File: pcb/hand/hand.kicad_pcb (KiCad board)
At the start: 2 copper layers, 178.2 x 125.2 mm, 43 parts, among them J1 Conn_01x15, J2 Conn_01x15

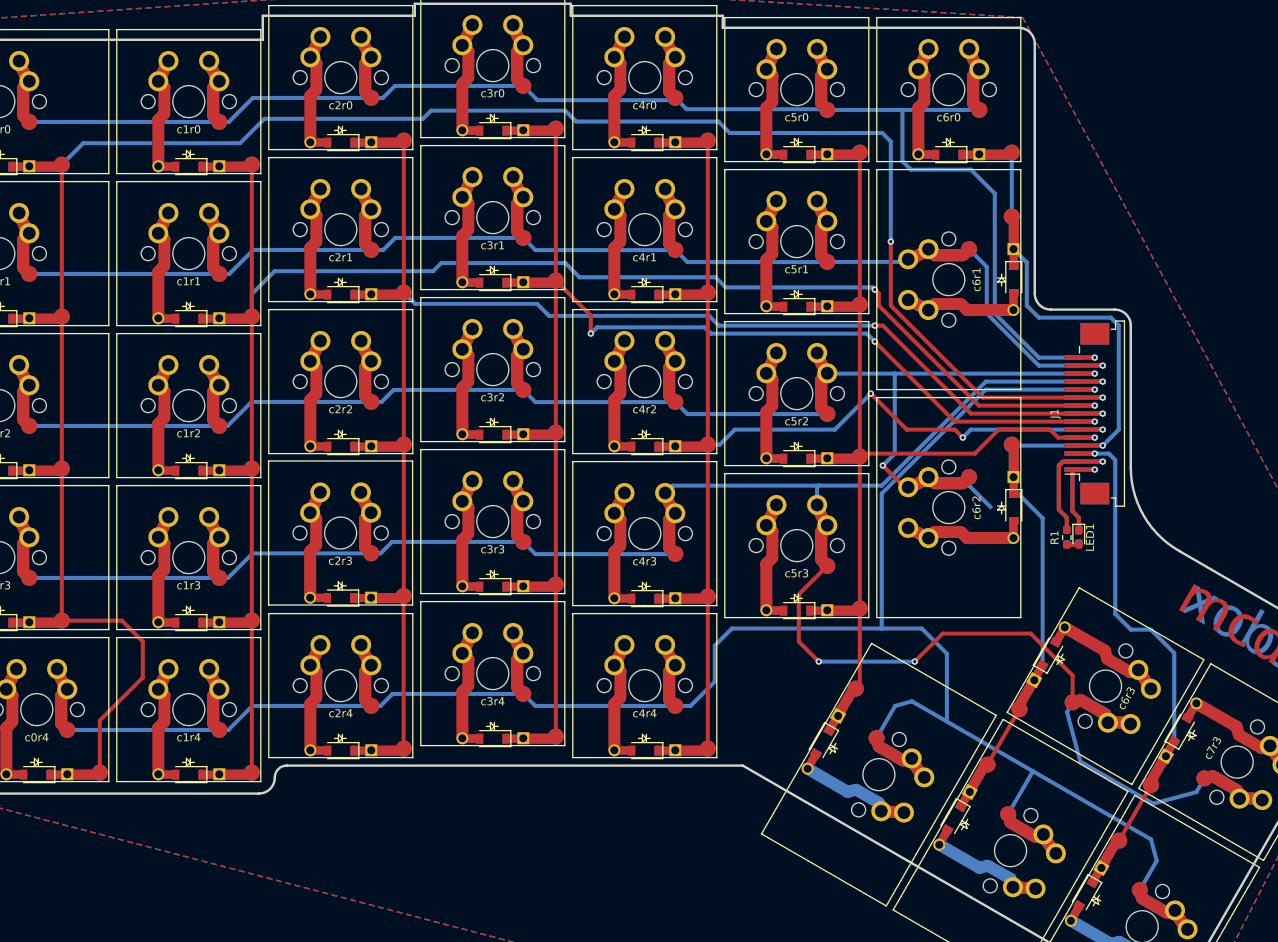
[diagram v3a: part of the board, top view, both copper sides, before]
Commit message: pcb/hand Mounting holes and archive footprints.
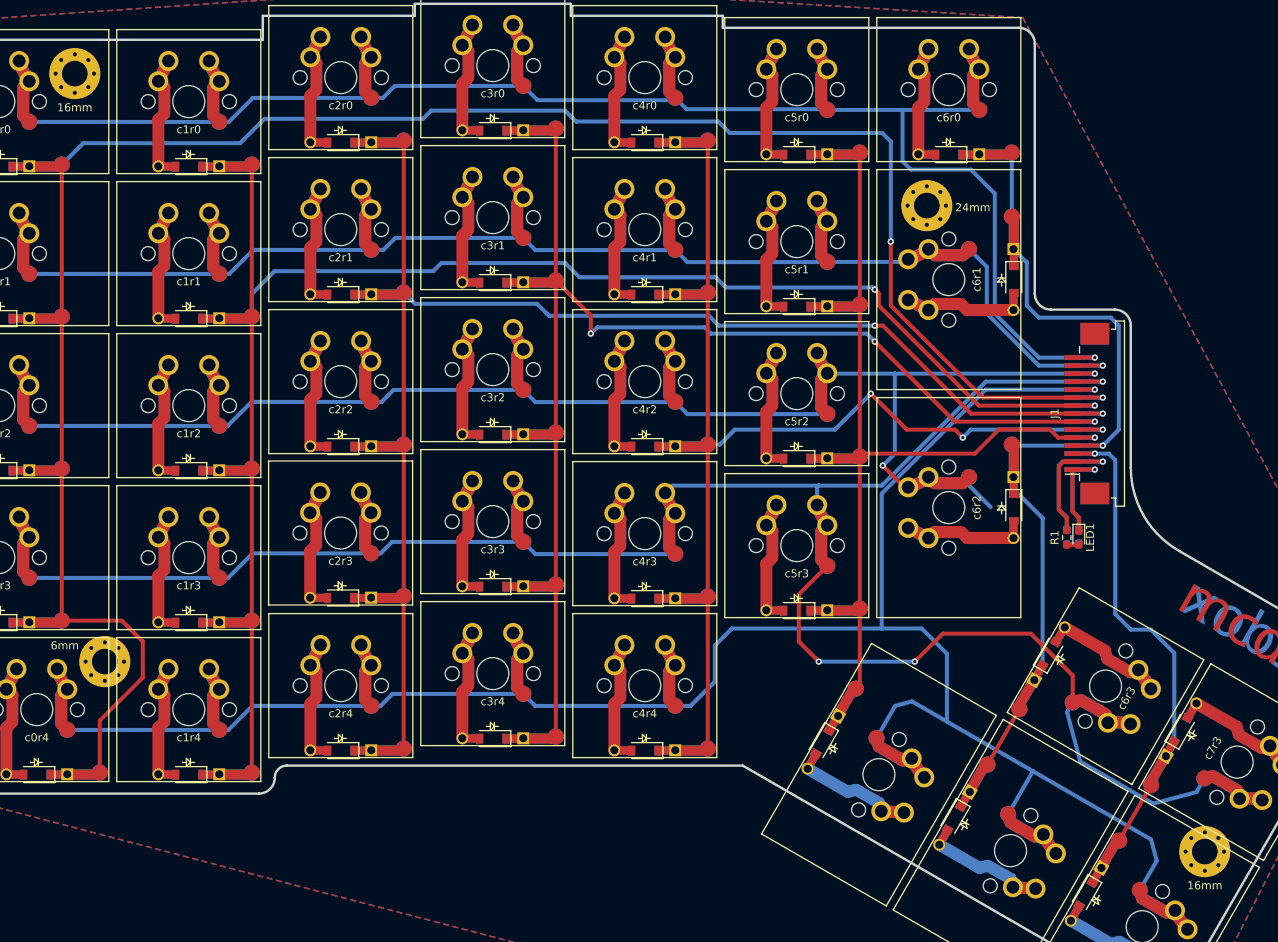
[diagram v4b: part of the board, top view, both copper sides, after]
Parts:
- added 16mm: MountingHole_3.2mm_M3_Pad_Via, MountingHole:MountingHole_3.2mm_M3_Pad_Via, F.Cu at (194.8, 132.8)
- added 16mm: MountingHole_3.2mm_M3_Pad_Via, MountingHole:MountingHole_3.2mm_M3_Pad_Via, F.Cu at (53.5, 35.5)
- added 24mm: MountingHole_3.2mm_M3_Pad_Via, MountingHole:MountingHole_3.2mm_M3_Pad_Via, F.Cu at (160.0, 52.0)
- added 6mm: MountingHole_3.2mm_M3_Pad_Via, MountingHole:MountingHole_3.2mm_M3_Pad_Via, F.Cu at (57.2, 109.0)
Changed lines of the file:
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@@
     (tracks 681)
     (zones 0)
-    (modules 43)
+    (modules 47)
     (nets 18)
   )
@@
     (38 B.Mask user hide)
     (39 F.Mask user hide)
-    (40 Dwgs.User user hide)
+    (40 Dwgs.User user)
     (41 Cmts.User user hide)
     (42 Eco1.User user hide)
@@
     (add_net row4)
   )
+  (module MountingHole:MountingHole_3.2mm_M3_Pad_Via (layer F.Cu)
+    (at 194.75 132.75)
+    (descr "Mounting Hole 3.2mm, M3")
+    (tags "mounting hole 3.2mm m3")
+    (attr virtual)
+    (fp_text reference 16mm (at 0 4.25) (layer F.SilkS)
+      (effects (font (size 1 1) (thickness 0.15)))
+    )
+    (fp_text value MountingHole_3.2mm_M3_Pad_Via (at 0 4.2) (layer F.Fab)
+      (effects (font (size 1 1) (thickness 0.15)))
+    )
+    (fp_text user %R (at 0.3 0) (layer F.Fab)
+      (effects (font (size 1 1) (thickness 0.15)))
+    )
+    (fp_circle (center 0 0) (end 3.2 0) (layer Cmts.User) (width 0.15))
+    (fp_circle (center 0 0) (end 3.45 0) (layer F.CrtYd) (width 0.05))
+    (pad 1 thru_hole circle (at 1.697056 -1.697056) (size 0.8 0.8) (drill 0.5) (layers *.Cu *.Mask))
+    (pad 1 thru_hole circle (at 0 -2.4) (size 0.8 0.8) (drill 0.5) (layers *.Cu *.Mask))
+    (pad 1 thru_hole circle (at -1.697056 -1.697056) (size 0.8 0.8) (drill 0.5) (layers *.Cu *.Mask))
+    (pad 1 thru_hole circle (at -2.4 0) (size 0.8 0.8) (drill 0.5) (layers *.Cu *.Mask))
+    (pad 1 thru_hole circle (at -1.697056 1.697056) (size 0.8 0.8) (drill 0.5) (layers *.Cu *.Mask))
+    (pad 1 thru_hole circle (at 0 2.4) (size 0.8 0.8) (drill 0.5) (layers *.Cu *.Mask))
+    (pad 1 thru_hole circle (at 1.697056 1.697056) (size 0.8 0.8) (drill 0.5) (layers *.Cu *.Mask))
+    (pad 1 thru_hole circle (at 2.4 0) (size 0.8 0.8) (drill 0.5) (layers *.Cu *.Mask))
+    (pad 1 thru_hole circle (at 0 0) (size 6.4 6.4) (drill 3.2) (layers *.Cu *.Mask))
+  )
+  (module MountingHole:MountingHole_3.2mm_M3_Pad_Via (layer F.Cu)
+    (at 57.25 109)
+    (descr "Mounting Hole 3.2mm, M3")
+    (tags "mounting hole 3.2mm m3")
+    (attr virtual)
+    (fp_text reference 6mm (at -5 -2) (layer F.SilkS)
+      (effects (font (size 1 1) (thickness 0.15)))
+    )
+    (fp_text value MountingHole_3.2mm_M3_Pad_Via (at 0 4.2) (layer F.Fab)
+      (effects (font (size 1 1) (thickness 0.15)))
+    )
+    (fp_text user %R (at 0.3 0) (layer F.Fab)
+      (effects (font (size 1 1) (thickness 0.15)))
+    )
+    (fp_circle (center 0 0) (end 3.2 0) (layer Cmts.User) (width 0.15))
+    (fp_circle (center 0 0) (end 3.45 0) (layer F.CrtYd) (width 0.05))
+    (pad 1 thru_hole circle (at 1.697056 -1.697056) (size 0.8 0.8) (drill 0.5) (layers *.Cu *.Mask))
+    (pad 1 thru_hole circle (at 0 -2.4) (size 0.8 0.8) (drill 0.5) (layers *.Cu *.Mask))
+    (pad 1 thru_hole circle (at -1.697056 -1.697056) (size 0.8 0.8) (drill 0.5) (layers *.Cu *.Mask))
+    (pad 1 thru_hole circle (at -2.4 0) (size 0.8 0.8) (drill 0.5) (layers *.Cu *.Mask))
+    (pad 1 thru_hole circle (at -1.697056 1.697056) (size 0.8 0.8) (drill 0.5) (layers *.Cu *.Mask))
+    (pad 1 thru_hole circle (at 0 2.4) (size 0.8 0.8) (drill 0.5) (layers *.Cu *.Mask))
+    (pad 1 thru_hole circle (at 1.697056 1.697056) (size 0.8 0.8) (drill 0.5) (layers *.Cu *.Mask))
+    (pad 1 thru_hole circle (at 2.4 0) (size 0.8 0.8) (drill 0.5) (layers *.Cu *.Mask))
+    (pad 1 thru_hole circle (at 0 0) (size 6.4 6.4) (drill 3.2) (layers *.Cu *.Mask))
+  )
+  (module MountingHole:MountingHole_3.2mm_M3_Pad_Via (layer F.Cu)
+    (at 160 52)
+    (descr "Mounting Hole 3.2mm, M3")
+    (tags "mounting hole 3.2mm m3")
+    (attr virtual)
+    (fp_text reference 24mm (at 5.75 0.25) (layer F.SilkS)
+      (effects (font (size 1 1) (thickness 0.15)))
+    )
+    (fp_text value MountingHole_3.2mm_M3_Pad_Via (at 0 4.2) (layer F.Fab)
+      (effects (font (size 1 1) (thickness 0.15)))
+    )
+    (fp_text user %R (at 0.3 0) (layer F.Fab)
+      (effects (font (size 1 1) (thickness 0.15)))
+    )
+    (fp_circle (center 0 0) (end 3.2 0) (layer Cmts.User) (width 0.15))
+    (fp_circle (center 0 0) (end 3.45 0) (layer F.CrtYd) (width 0.05))
+    (pad 1 thru_hole circle (at 1.697056 -1.697056) (size 0.8 0.8) (drill 0.5) (layers *.Cu *.Mask))
+    (pad 1 thru_hole circle (at 0 -2.4) (size 0.8 0.8) (drill 0.5) (layers *.Cu *.Mask))
+    (pad 1 thru_hole circle (at -1.697056 -1.697056) (size 0.8 0.8) (drill 0.5) (layers *.Cu *.Mask))
+    (pad 1 thru_hole circle (at -2.4 0) (size 0.8 0.8) (drill 0.5) (layers *.Cu *.Mask))
+    (pad 1 thru_hole circle (at -1.697056 1.697056) (size 0.8 0.8) (drill 0.5) (layers *.Cu *.Mask))
+    (pad 1 thru_hole circle (at 0 2.4) (size 0.8 0.8) (drill 0.5) (layers *.Cu *.Mask))
+    (pad 1 thru_hole circle (at 1.697056 1.697056) (size 0.8 0.8) (drill 0.5) (layers *.Cu *.Mask))
+    (pad 1 thru_hole circle (at 2.4 0) (size 0.8 0.8) (drill 0.5) (layers *.Cu *.Mask))
+    (pad 1 thru_hole circle (at 0 0) (size 6.4 6.4) (drill 3.2) (layers *.Cu *.Mask))
+  )
+  (module MountingHole:MountingHole_3.2mm_M3_Pad_Via (layer F.Cu)
+    (at 53.5 35.5)
+    (descr "Mounting Hole 3.2mm, M3")
+    (tags "mounting hole 3.2mm m3")
+    (attr virtual)
+    (fp_text reference 16mm (at 0 4.25) (layer F.SilkS)
+      (effects (font (size 1 1) (thickness 0.15)))
+    )
+    (fp_text value MountingHole_3.2mm_M3_Pad_Via (at 0 4.2) (layer F.Fab)
+      (effects (font (size 1 1) (thickness 0.15)))
+    )
+    (fp_text user %R (at 0.3 0) (layer F.Fab)
+      (effects (font (size 1 1) (thickness 0.15)))
+    )
+    (fp_circle (center 0 0) (end 3.2 0) (layer Cmts.User) (width 0.15))
+    (fp_circle (center 0 0) (end 3.45 0) (layer F.CrtYd) (width 0.05))
+    (pad 1 thru_hole circle (at 1.697056 -1.697056) (size 0.8 0.8) (drill 0.5) (layers *.Cu *.Mask))
+    (pad 1 thru_hole circle (at 0 -2.4) (size 0.8 0.8) (drill 0.5) (layers *.Cu *.Mask))
+    (pad 1 thru_hole circle (at -1.697056 -1.697056) (size 0.8 0.8) (drill 0.5) (layers *.Cu *.Mask))
+    (pad 1 thru_hole circle (at -2.4 0) (size 0.8 0.8) (drill 0.5) (layers *.Cu *.Mask))
+    (pad 1 thru_hole circle (at -1.697056 1.697056) (size 0.8 0.8) (drill 0.5) (layers *.Cu *.Mask))
+    (pad 1 thru_hole circle (at 0 2.4) (size 0.8 0.8) (drill 0.5) (layers *.Cu *.Mask))
+    (pad 1 thru_hole circle (at 1.697056 1.697056) (size 0.8 0.8) (drill 0.5) (layers *.Cu *.Mask))
+    (pad 1 thru_hole circle (at 2.4 0) (size 0.8 0.8) (drill 0.5) (layers *.Cu *.Mask))
+    (pad 1 thru_hole circle (at 0 0) (size 6.4 6.4) (drill 3.2) (layers *.Cu *.Mask))
+  )
   (module hand:reversibleMX_15u (layer B.Cu)
     (at 186.923019 142.133714 60)
@@
   (gr_line (start 191.25 151) (end 214.48205 110.75) (layer Edge.Cuts) (width 0.3))
   (gr_line (start 137 122) (end 188.51795 151.73205) (layer Edge.Cuts) (width 0.3))
-  (gr_line (start 121.1 95.7) (end 160 52) (layer Dwgs.User) (width 0.15))
-  (gr_line (start 57 109) (end 91.9 69.8) (layer Dwgs.User) (width 0.15))
-  (gr_line (start 53.5 35.5) (end 172.5 141.5) (layer Dwgs.User) (width 0.15))
+  (gr_line (start 133.5 90.5) (end 160 52) (layer Dwgs.User) (width 0.15))
+  (gr_line (start 57 109) (end 90 60.75) (layer Dwgs.User) (width 0.15))
+  (gr_line (start 53.5 35.5) (end 194.75 132.75) (layer Dwgs.User) (width 0.15))
   (gr_text mcdox (at 202.562599 106.238221 -30) (layer B.Cu)
     (effects (font (size 5 5) (thickness 0.3)) (justify mirror))
